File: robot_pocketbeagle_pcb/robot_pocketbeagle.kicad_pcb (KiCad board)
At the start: 2 copper layers, 75 x 100 mm, 76 parts, among them J1 QMC5883L, J10 driver_dvr8833, J11 12V_DC, J12 IN_DVR8833, J13 9V_DC_DC, J14 servo_x_y, J15 shr05, J16 5V_DC_DC, J17 Conn_GND, J18 Conn_5V, J19 Conn_pwm_out_b, J2 USB_A, J20 Conn_pwm_out_a, J21 Conn_P2_3.3V, J26 Conn_12.6V, J29 Conn_AIN_4.096_3.3_1.8V, J3 UART0, J30 Conn_5V, J31 Conn_GPI028_34, J4 P1, J5 MPU6050, J6 ADS1115, J7 P2, J8 Conn_i2c2, J9 OUT_DVR8833, Q1 BC847, Q2 D90N02L, Q3 D90N02L, U1 PC817, U2 PC817, U3 74HC00, U4 LM358

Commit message: update pcb
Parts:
- removed J11: 12V_DC, TerminalBlock:TerminalBlock_bornier-2_P5.08mm
- removed J26: Conn_12.6V, Connector_PinSocket_2.54mm:PinSocket_1x02_P2.54mm_Vertical
- added C3: 100n, Capacitor_SMD:C_0805_2012Metric, B.Cu at (141.5, 118.1)
- added C4: 100n, Capacitor_SMD:C_0805_2012Metric, B.Cu at (139.4, 118.0)
- added C5: 33n, Capacitor_SMD:C_0805_2012Metric, B.Cu at (121.3, 123.8)
- added C6: 1n, Capacitor_SMD:C_0805_2012Metric, B.Cu at (121.3, 120.2)
- added D1: LED, LED_THT:LED_D3.0mm, F.Cu at (106.0, 65.4)
- added Q4: BC847, Package_TO_SOT_SMD:SOT-23, B.Cu at (126.4, 113.0)
- added Q5: BC847, Package_TO_SOT_SMD:SOT-23, B.Cu at (104.6, 99.2)
- added Q6: QM6015D, Package_TO_SOT_SMD:TO-252-2, B.Cu at (118.7, 111.4)
- added Q7: QM6015D, Package_TO_SOT_SMD:TO-252-2, B.Cu at (112.4, 97.8)
- added R38: 27, Resistor_SMD:R_0805_2012Metric, B.Cu at (147.7, 65.4)
- added R39: 27, Resistor_SMD:R_0805_2012Metric, B.Cu at (147.7, 70.5)
- added R40: 0, Resistor_SMD:R_1206_3216Metric, B.Cu at (160.1, 120.7)
- added R41: 2K, Resistor_SMD:R_0805_2012Metric, B.Cu at (108.0, 71.5)
- added R42: 1K, Resistor_SMD:R_0805_2012Metric, B.Cu at (118.2, 102.6)
- added R43: 100K, Resistor_SMD:R_0805_2012Metric, B.Cu at (108.3, 106.3)
- added R44: 1K, Resistor_SMD:R_0805_2012Metric, B.Cu at (126.4, 109.2)
- added R45: 1K, Resistor_SMD:R_0805_2012Metric, B.Cu at (104.6, 95.5)
- added R46: 100K, Resistor_SMD:R_0805_2012Metric, B.Cu at (130.2, 114.0)
- added R47: 100K, Resistor_SMD:R_0805_2012Metric, B.Cu at (108.6, 98.2)
- added R48: 0, Resistor_SMD:R_0805_2012Metric, B.Cu at (118.2, 104.5)
- added R49: 0, Resistor_SMD:R_0805_2012Metric, B.Cu at (126.4, 106.5)
- added R51: 0, Resistor_SMD:R_0805_2012Metric, B.Cu at (130.3, 94.6)
- added R52: 0, Resistor_SMD:R_1206_3216Metric, B.Cu at (133.2, 115.9)
- added R53: 0, Resistor_SMD:R_1206_3216Metric, B.Cu at (136.2, 118.9)
- added R54: 0, Resistor_SMD:R_1206_3216Metric, B.Cu at (136.2, 114.7)
- added U5: L7805_REZERV, Package_TO_SOT_SMD:TO-252-2, B.Cu at (128.6, 122.0)
- Q2: value D90N02L -> BC847; footprint Package_TO_SOT_SMD:TO-252-2 -> Package_TO_SOT_SMD:SOT-23
- Q3: value D90N02L -> QM6015D
- R18, R30: value 47K -> 110K
- R21: value 0,1 -> 100K; footprint Resistor_SMD:R_1206_3216Metric -> Resistor_SMD:R_0805_2012Metric
- R31: value 250 -> 100K
- R33, R34, R35, R36, R37: value 0,1 -> 0
- moved R16 20.2 mm to (132.4, 94.7)
- moved R18 18.6 mm to (134.3, 110.5), turned to 180 degrees
- moved R31 17.4 mm to (137.9, 97.6), turned to 90 degrees
- moved R30 17.1 mm to (137.1, 100.5), turned to 0 degrees
- moved R27 16.8 mm to (134.7, 94.6), turned to -90 degrees
- moved R17 14.9 mm to (137.6, 93.7), turned to 180 degrees
- moved J13 13.3 mm to (112.4, 123.2)
- moved Q3 11.9 mm to (108.8, 110.2), turned to -90 degrees
- moved R21 8.87 mm to (130.7, 110.5)
- moved Q2 6.50 mm to (114.4, 103.5)
- moved U3 6.03 mm to (125.4, 100.3)
- moved C1 5.34 mm to (122.9, 93.8)
- moved R6 4.53 mm to (167.3, 102.2)
- moved C2 4.08 mm to (138.5, 103.8)
- moved U4 4.02 mm to (134.3, 105.5)
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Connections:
- net P1_DN_USB renamed P1_USB_D_N
- net P1_DP_USB renamed P1_USB_D_P
- C1 pad 1: P1_SYS_VIN -> AUX_5V_OUT
- C1 pad 2: GND_SYS -> GND
- C2 pad 1: P1_SYS_VIN -> 12.6V_BAT_IN
- C2 pad 2: GND_SYS -> GND
- H1 pad 1: unconnected-(H1-Pad1) -> GND
- H2 pad 1: unconnected-(H2-Pad1) -> GND
- H3 pad 1: unconnected-(H3-Pad1) -> GND
- H4 pad 1: unconnected-(H4-Pad1) -> GND
- J1 pad 2: GND_SYS -> GND
- J12 pad 8: GND_SYS -> GND
- J13 pad 1: 12.6V_BAT_IN -> 9V_DRIVER_DC_DC_IN
- J13 pad 2: 9V_DRIVER_DC_DC -> 12.6V_BAT_IN
- J14 pad 3: GND_SYS -> GND
- J14 pad 6: GND_SYS -> GND
- J15 pad 4: GND_SYS -> GND
- J16 pad 1: GND_SYS -> GND
- J16 pad 2: Net-(J16-Pad2) -> 5V_SYS_VIN_IN
- J17 pad 1: GND_SYS -> GND
- J17 pad 2: GND_SYS -> GND
- J17 pad 3: GND_SYS -> GND
- J17 pad 4: GND_SYS -> GND
- J17 pad 5: GND_SYS -> GND
- J17 pad 6: GND_SYS -> GND
- J17 pad 7: GND_SYS -> GND
- J17 pad 8: GND_SYS -> GND
- J17 pad 9: GND_SYS -> GND
- J18 pad 1: P1_SYS_VIN -> 5V_SYS_VIN_IN
- J18 pad 2: Net-(J16-Pad2) -> 5V_SYS_VIN_IN
- J2 pad 4: GND_SYS -> GND
- J2 pad 5: GND_SYS -> GND
- J3 pad 1: GND_SYS -> GND
- J4 pad 13: GND_SYS -> P1_ID_USB
- J4 pad 15: GND_SYS -> P1_ID_USB
- J4 pad 16: GND_SYS -> GND
- J4 pad 22: GND_SYS -> GND
- J5 pad 2: GND_SYS -> GND
- J6 pad 2: GND_SYS -> GND
- J7 pad 15: GND_SYS -> GND
- J7 pad 21: GND_SYS -> GND
- J8 pad 2: GND_SYS -> GND
- J9 pad 1: 9V_DRIVER_DC_DC -> 9V_DRIVER_DC_DC_OUT
- J9 pad 8: Net-(J9-Pad8) -> GND
- Q1 pad 2: GND_SYS -> GND
- Q2 pad 2: Net-(J26-Pad1) -> GND
- Q2 pad 3: GND_BAT -> Net-(Q2-Pad3)
- Q3 pad 1: Net-(Q3-Pad1) -> Net-(Q2-Pad3)
- Q3 pad 2: Net-(J9-Pad8) -> AUX_5V_OUT
- Q3 pad 3: GND_SYS -> P1_SYS_VIN
- R10 pad 2: 9V_DRIVER_DC_DC -> 9V_DRIVER_DC_DC_IN
- R11 pad 1: GND_SYS -> GND
- R13 pad 1: GND_SYS -> GND
- R15 pad 1: GND_SYS -> GND
- R16 pad 2: 9V_DRIVER_DC_DC -> 9V_DRIVER_DC_DC_IN
- R17 pad 1: GND_SYS -> GND
- R18 pad 1: GND_SYS -> Net-(R18-Pad1)
- R18 pad 2: Net-(Q2-Pad1) -> Net-(R18-Pad2)
- R20 pad 2: GND_SYS -> GND
- R21 pad 1: 12.6V_BAT_IN -> Net-(R18-Pad2)
- R21 pad 2: Net-(J26-Pad1) -> GND
- R22 pad 1: GND_SYS -> GND
- R30 pad 1: Net-(Q3-Pad1) -> Net-(R30-Pad1)
- R30 pad 2: GND_SYS -> Net-(R30-Pad2)
- R31 pad 1: P1_SYS_VIN -> Net-(R30-Pad2)
- R31 pad 2: Net-(R31-Pad2) -> GND
- R33 pad 1: GND_SYS -> GND
- R33 pad 2: GND_SYS -> GND
- R34 pad 1: GND_SYS -> GND
- R34 pad 2: GND_SYS -> GND
- R35 pad 1: GND_SYS -> GND
- R35 pad 2: GND_SYS -> GND
- R9 pad 1: GND_SYS -> GND
- U1 pad 2: GND_SYS -> GND
- U1 pad 3: GND_SYS -> GND
- U2 pad 2: GND_SYS -> GND
- U2 pad 3: GND_SYS -> GND
- U3 pad 1: Net-(U3-Pad1) -> Net-(R18-Pad2)
- U3 pad 10: (no net) -> P2_GPIO9_OUT_mosfet
- U3 pad 11: Net-(Q3-Pad1) -> Net-(R45-Pad1)
- U3 pad 12: P2_GPIO9_OUT_mosfet -> Net-(U3-Pad12)
- U3 pad 13: Net-(R31-Pad2) -> Net-(U3-Pad12)
- U3 pad 14: P1_SYS_VIN -> AUX_5V_OUT
- U3 pad 2: Net-(U3-Pad2) -> Net-(R18-Pad2)
- U3 pad 3: Net-(Q2-Pad1) -> Net-(R42-Pad2)
- U3 pad 4: (no net) -> Net-(R42-Pad2)
- U3 pad 5: (no net) -> Net-(R42-Pad2)
- U3 pad 6: (no net) -> Net-(R44-Pad1)
- U3 pad 7: GND_SYS -> GND
- U3 pad 8: (no net) -> Net-(U3-Pad12)
- U3 pad 9: (no net) -> Net-(R30-Pad2)
- U4 pad 1: Net-(U3-Pad1) -> Net-(R18-Pad1)
- U4 pad 4: GND_SYS -> GND
- U4 pad 7: Net-(U3-Pad2) -> Net-(R30-Pad1)
- U4 pad 8: P1_SYS_VIN -> 12.6V_BAT_IN
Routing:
- net 9V_DRIVER_DC_DC: track 102.5 -> 0.00 mm, vias 2 -> 0
- net 9V_DRIVER_DC_DC_IN: track 0.00 -> 56.7 mm, vias 0 -> 4
- net AUX_5V_OUT: track 0.00 -> 51.1 mm
- net 5V_SYS_VIN_IN: track 0.00 -> 42.7 mm
- net 9V_DRIVER_DC_DC_OUT: track 0.00 -> 30.3 mm
- net Net-(R45-Pad1): track 0.00 -> 29.0 mm
- net Net-(R30-Pad2): track 0.00 -> 25.7 mm
- net Net-(Q2-Pad1): track 25.4 -> 1.96 mm
- net Net-(U3-Pad1): track 19.8 -> 0.00 mm
- net Net-(J26-Pad1): track 19.4 -> 0.00 mm
- net Net-(Q3-Pad1): track 18.2 -> 0.00 mm
- net 12.6V_BAT_IN: track 15.8 -> 33.4 mm, vias 2 -> 3
- net Net-(R18-Pad2): track 0.00 -> 17.5 mm
- net Net-(U3-Pad2): track 16.4 -> 0.00 mm
- net Net-(R42-Pad2): track 0.00 -> 15.6 mm
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- added copper zone on B.Cu, net GND
- removed copper zone on B.Cu, net GND_SYS

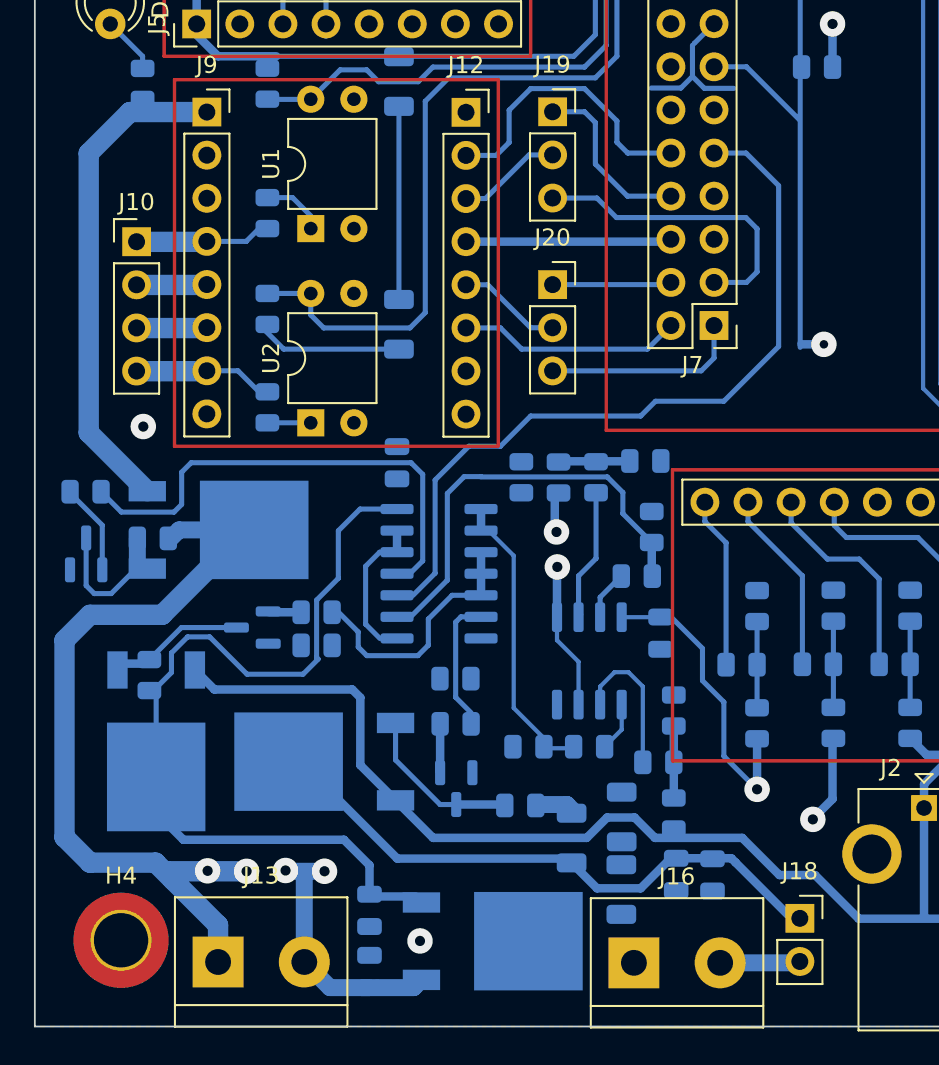
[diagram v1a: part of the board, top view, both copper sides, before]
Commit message: add sim. shem and fix board shem
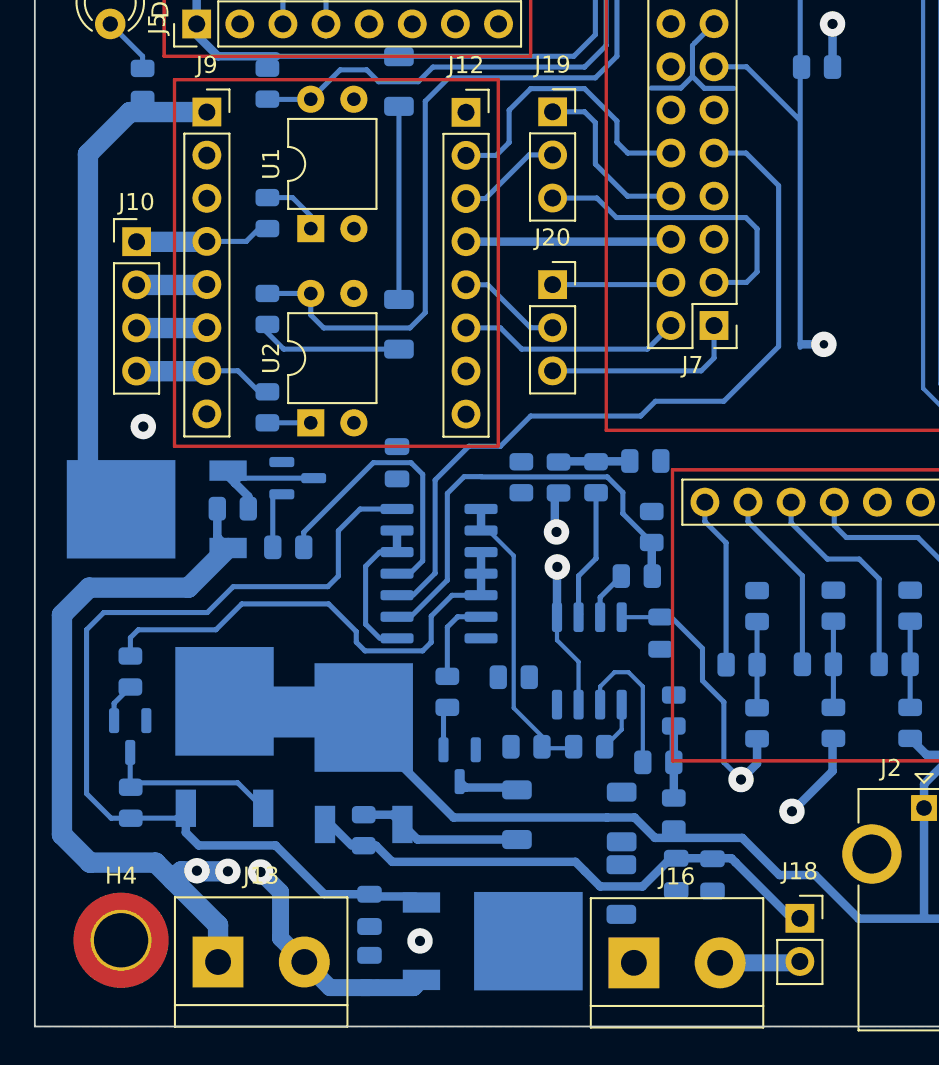
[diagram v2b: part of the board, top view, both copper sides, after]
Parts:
- removed R48: 0, Resistor_SMD:R_0805_2012Metric
- removed R52: 0, Resistor_SMD:R_1206_3216Metric
- added R50: 0, Resistor_SMD:R_1206_3216Metric, B.Cu at (130.0, 114.5)
- moved Q5 13.2 mm to (117.1, 94.7), turned to 0 degrees
- moved R45 12.4 mm to (116.5, 98.8)
- moved R42 11.5 mm to (107.2, 106.1), turned to 90 degrees
- moved Q2 9.64 mm to (107.2, 109.9), turned to -90 degrees
- moved R46 9.34 mm to (121.0, 115.4), turned to 90 degrees
- moved R43 7.60 mm to (107.2, 113.8)
- moved R47 5.02 mm to (113.3, 96.5), turned to 0 degrees
- moved Q3 4.03 mm to (112.8, 109.9), turned to 90 degrees
- moved Q7 3.84 mm to (108.8, 96.5), turned to 180 degrees
- moved R49 3.44 mm to (129.8, 106.4)
- moved Q6 2.38 mm to (121.0, 110.9), turned to 90 degrees
- moved R44 1.95 mm to (125.9, 107.3), turned to -90 degrees
- moved Q4 1.36 mm to (126.6, 111.6)
- moved R21 0.12 mm to (130.6, 110.5)
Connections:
- Q3 pad 2: AUX_5V_OUT -> P1_SYS_VIN
- Q3 pad 3: P1_SYS_VIN -> AUX_5V_OUT
- Q6 pad 1: Net-(Q4-Pad3) -> Net-(Q6-Pad1)
- Q6 pad 2: 5V_SYS_VIN_IN -> P1_SYS_VIN
- Q6 pad 3: P1_SYS_VIN -> 5V_SYS_VIN_IN
- Q7 pad 2: 9V_DRIVER_DC_DC_IN -> 9V_DRIVER_DC_DC_OUT
- Q7 pad 3: 9V_DRIVER_DC_DC_OUT -> 9V_DRIVER_DC_DC_IN
- R46 pad 2: Net-(Q4-Pad3) -> Net-(Q6-Pad1)
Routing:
- net Net-(R42-Pad2): track 15.6 -> 28.9 mm
- net Net-(R45-Pad1): track 29.0 -> 16.8 mm
- net Net-(Q6-Pad1): track 0.00 -> 9.63 mm
- net Net-(Q4-Pad3): track 9.86 -> 3.58 mm
- net 5V_SYS_VIN_IN: track 42.7 -> 36.6 mm
- net P1_SYS_VIN: track 385.2 -> 379.9 mm
- net AUX_5V_OUT: track 51.1 -> 56.2 mm
- net 9V_DRIVER_DC_DC_IN: track 56.7 -> 52.8 mm
- net Net-(R44-Pad1): track 8.00 -> 5.14 mm
- net 12.6V_BAT_IN: track 33.4 -> 30.9 mm, vias 3 -> 2
- net Net-(Q5-Pad1): track 5.39 -> 3.10 mm
- net Net-(Q2-Pad3): track 8.34 -> 10.6 mm
- net Net-(Q5-Pad3): track 9.23 -> 7.16 mm
- net 9V_DRIVER_DC_DC_OUT: track 30.3 -> 29.8 mm

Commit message: fix board
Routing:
- net Net-(J2-Pad2): track 14.4 -> 15.0 mm
- net Net-(J2-Pad3): track 17.0 -> 17.5 mm

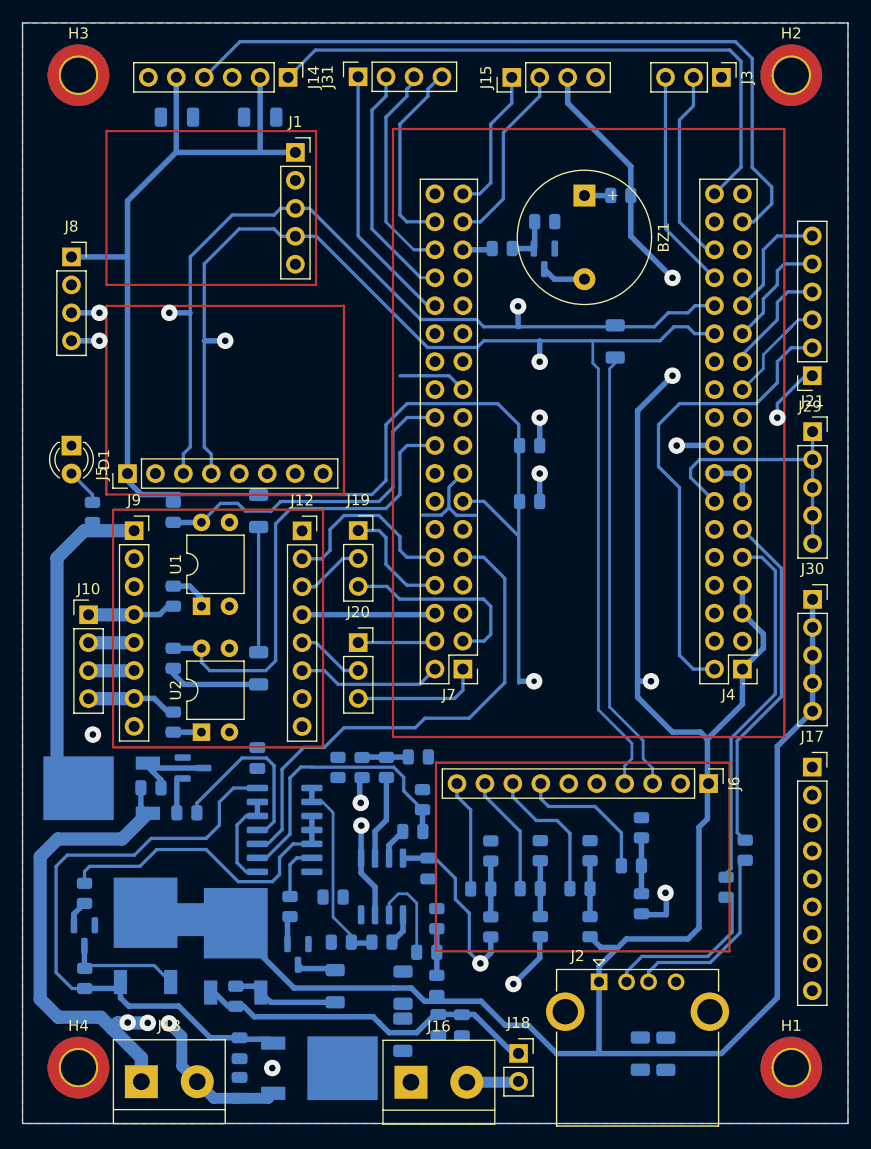
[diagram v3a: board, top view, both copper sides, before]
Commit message: fix board optopara
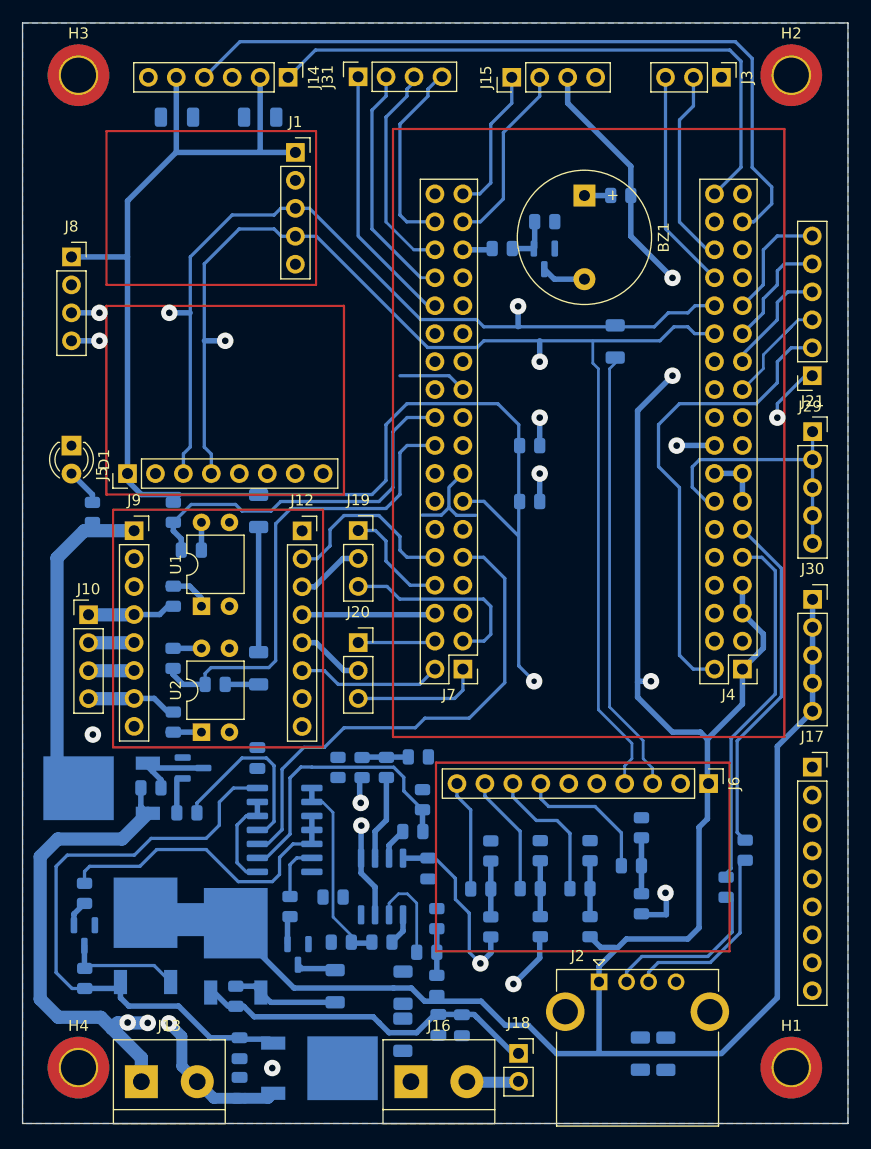
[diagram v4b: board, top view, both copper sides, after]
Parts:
- added R48: 90k, Resistor_SMD:R_0805_2012Metric, B.Cu at (116.9, 74.9)
- added R52: 90k, Resistor_SMD:R_0805_2012Metric, B.Cu at (115.3, 84.7)
- R4, R5: value 1K -> 47k
- moved R5 4.48 mm to (119.1, 87.1), turned to 0 degrees
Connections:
- U1 pad 4: P2_GPIO20_DRIVER_OPTO_OUTA1 -> Net-(U1-Pad4)
- U2 pad 4: P2_GPIO18_DRIVER_OPTO_OUTB1 -> Net-(U2-Pad4)
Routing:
- net P1_SYS_VIN: track 379.9 -> 373.1 mm
- net Net-(U2-Pad4): track 0.00 -> 2.58 mm
- net Net-(U1-Pad4): track 0.00 -> 2.52 mm
- net P2_GPIO20_DRIVER_OPTO_OUTA1: track 31.9 -> 34.0 mm

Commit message: board debugging
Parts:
- added R55: 1K, Resistor_SMD:R_0805_2012Metric, B.Cu at (108.1, 106.1)
- added R56: 1K, Resistor_SMD:R_0805_2012Metric, B.Cu at (128.5, 108.3)
- added R57: 1K, Resistor_SMD:R_0805_2012Metric, B.Cu at (120.2, 94.7)
- moved R42 1.09 mm to (106.1, 106.1)
- moved R49 0.28 mm to (129.8, 106.2)
- moved R44 0.27 mm to (125.7, 107.4)
- moved R43 0.10 mm to (107.2, 113.8)
- moved Q2 0.09 mm to (107.1, 109.9)
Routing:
- net Net-(Q5-Pad1): track 3.10 -> 7.15 mm
- net Net-(Q2-Pad1): track 2.38 -> 4.70 mm
- net Net-(Q4-Pad1): track 2.59 -> 4.30 mm
- net Net-(R45-Pad1): track 16.8 -> 17.9 mm
- net Net-(R42-Pad2): track 28.6 -> 29.6 mm

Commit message: board debugging 1
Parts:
- moved R38 0.93 mm to (148.6, 65.4)
- moved R39 0.93 mm to (148.6, 70.5)
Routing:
- net P1_SYS_VIN: track 373.1 -> 375.1 mm
- net AUX_5V_OUT: track 55.5 -> 56.7 mm, vias 0 -> 1
- net 9V_DRIVER_DC_DC_IN: track 52.8 -> 51.8 mm
